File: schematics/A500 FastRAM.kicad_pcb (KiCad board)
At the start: 2 copper layers, 87.6 x 87.6 mm, 31 parts, among them J1 Microsemi_FlashPro-JTAG-10, U1 68000 Boardside, U10 TPS7333QP, U2 68000 Socket, U3 ATF1502ASV-15JU44, U4 74157, U5 74157, U6 IS41LV16100D, U7 IS41LV16100D, U8 IS41LV16100D, U9 IS41LV16100D

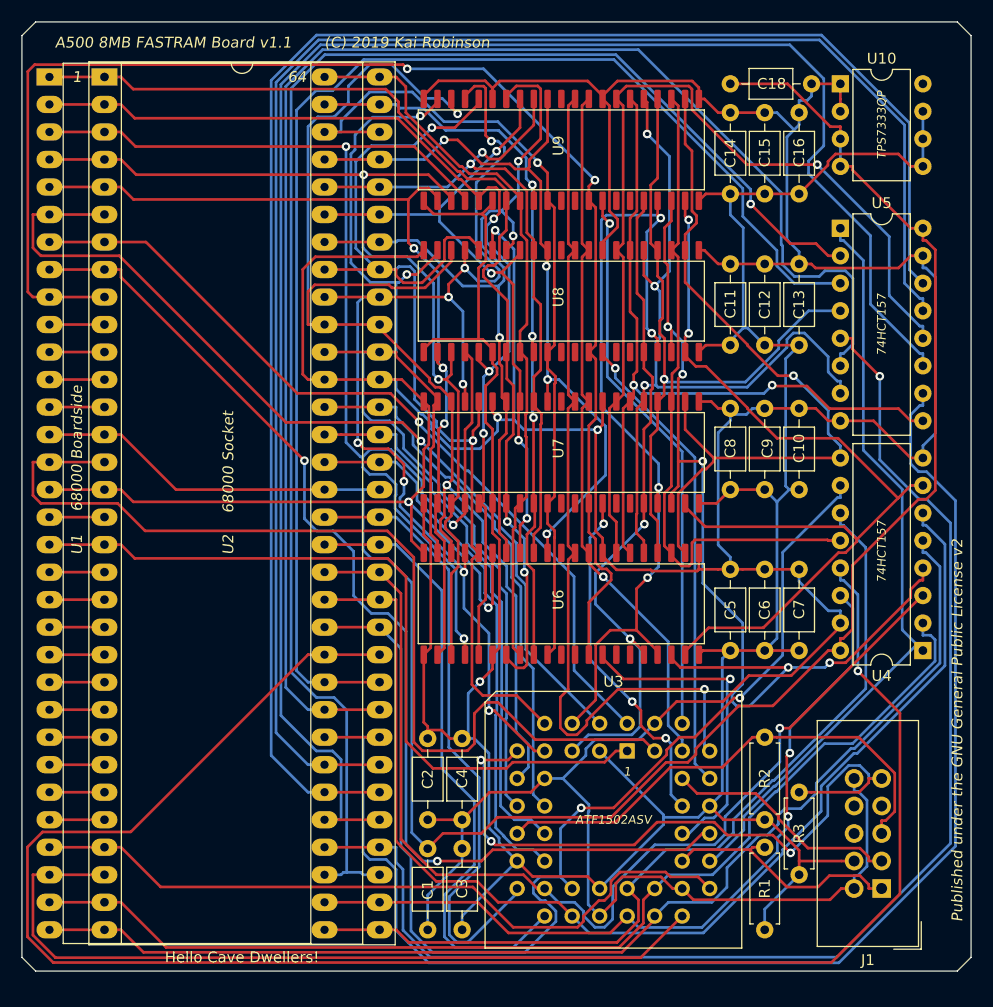
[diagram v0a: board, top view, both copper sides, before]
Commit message: Version 2
Swapped some components to SMD, reduced size of board - stepping stone to full blown accelerator integration!
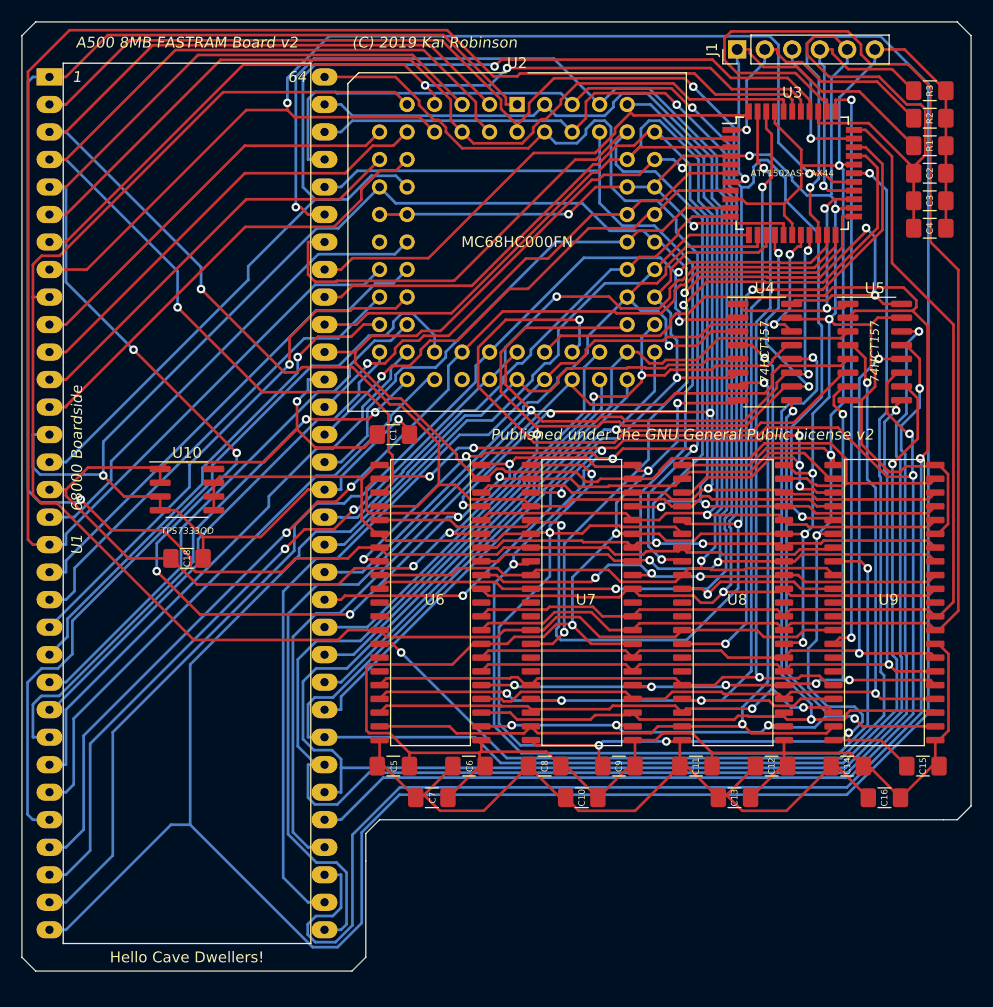
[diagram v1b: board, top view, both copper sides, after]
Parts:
- C1, C10, C11, C12, C13, C14, C15, C16, C18, C2, C3, C4, C5, C6, C7, C8, C9: footprint Capacitor_THT:C_Axial_L3.8mm_D2.6mm_P7.50mm_Horizontal -> Capacitor_SMD:C_1206_3216Metric_Pad1.42x1.75mm_HandSolder
- J1: value Microsemi_FlashPro-JTAG-10 -> Conn_01x06_Male; footprint Connector_IDC:IDC-Header_2x05_P2.54mm_Vertical -> Connector_PinHeader_2.54mm:PinHeader_1x06_P2.54mm_Vertical
- R1, R2, R3: footprint Resistor_THT:R_Axial_DIN0207_L6.3mm_D2.5mm_P7.62mm_Horizontal -> Resistor_SMD:R_1206_3216Metric_Pad1.42x1.75mm_HandSolder
- U10: value TPS7333QP -> TPS7333QD; footprint Package_DIP:DIP-8_W7.62mm -> Package_SO:SOIC-8_3.9x4.9mm_P1.27mm
- U2: value 68000 Socket -> MC68000FN; footprint Package_DIP:DIP-64_W25.4mm_Socket_LongPads -> Package_LCC:PLCC-68_THT-Socket
- U3: value ATF1502ASV-15JU44 -> ATF1502AS-7AX44; footprint Package_LCC:PLCC-44_THT-Socket -> Package_QFP:TQFP-44_10x10mm_P0.8mm
- U4, U5: footprint Package_DIP:DIP-16_W7.62mm -> Package_SO:SOIC-16_3.9x9.9mm_P1.27mm
- moved C3 80.0 mm to (201.9, 47.0), turned to 180 degrees
- moved J1 78.6 mm to (184.2, 33.0), turned to 90 degrees
- moved C2 75.6 mm to (201.9, 44.5), turned to 0 degrees
- moved R1 74.0 mm to (201.9, 41.9), turned to 180 degrees
- moved R3 73.4 mm to (201.9, 36.8), turned to 180 degrees
- moved U10 71.0 mm to (133.3, 73.7)
- moved C4 69.6 mm to (201.9, 49.5), turned to 0 degrees
- moved C18 66.6 mm to (133.3, 80.0), turned to 180 degrees
- moved R2 66.5 mm to (201.9, 39.4), turned to 180 degrees
- moved C16 56.3 mm to (197.7, 102.1), turned to 0 degrees
- moved U3 55.5 mm to (189.2, 44.5)
- moved C15 54.8 mm to (201.3, 99.2), turned to 0 degrees
- moved C14 53.9 mm to (194.3, 99.2), turned to 0 degrees
- moved U9 51.6 mm to (198.1, 82.5), turned to 0 degrees
- moved C13 42.2 mm to (183.9, 102.1), turned to 0 degrees
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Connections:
- J1 pad 1: /TCK -> /TMS
- J1 pad 2: GND -> /TDI
- J1 pad 4: /VCC33 -> /TCK
- J1 pad 5: /TMS -> GND
- J1 pad 6: Net-(J1-Pad6) -> /VCC33
- R1 pad 2: /TCK -> /TMS
- R2 pad 2: /TMS -> /TDI
- R3 pad 2: /TDI -> /TCK
- U2 pad 17: /CPU_HALT -> GND
- U2 pad 18: /CPU_RESET -> Net-(U2-Pad18)
- U2 pad 19: /CPU_VMA -> /CPU_HALT
- U2 pad 20: /CPU_E -> /CPU_RESET
- U2 pad 21: /CPU_VPA -> /CPU_VMA
- U2 pad 22: /CPU_BERR -> /CPU_E
- U2 pad 23: /CPU_IPL2 -> /CPU_VPA
- U2 pad 24: /CPU_IPL1 -> /CPU_BERR
- U2 pad 25: /CPU_IPL0 -> /CPU_IPL2
- U2 pad 26: /CPU_FC2 -> /CPU_IPL1
- U2 pad 27: /CPU_FC1 -> /CPU_IPL0
- U2 pad 28: /CPU_FC0 -> /CPU_FC2
- U2 pad 29: /CPU_A1 -> /CPU_FC1
- U2 pad 30: /CPU_A2 -> /CPU_FC0
- U2 pad 31: /CPU_A3 -> Net-(U2-Pad31)
- U2 pad 32: /CPU_A4 -> /CPU_A1
- U2 pad 33: /CPU_A5 -> /CPU_A2
- U2 pad 34: /CPU_A6 -> /CPU_A3
- U2 pad 35: /CPU_A7 -> /CPU_A4
- U2 pad 36: /CPU_A8 -> /CPU_A5
- U2 pad 37: /CPU_A9 -> /CPU_A6
- U2 pad 38: /CPU_A10 -> /CPU_A7
- U2 pad 39: /CPU_A11 -> /CPU_A8
- U2 pad 40: /CPU_A12 -> /CPU_A9
- U2 pad 41: /CPU_A13 -> /CPU_A10
- U2 pad 42: /CPU_A14 -> /CPU_A11
- U2 pad 43: /CPU_A15 -> /CPU_A12
- U2 pad 44: /CPU_A16 -> /CPU_A13
- U2 pad 45: /CPU_A17 -> /CPU_A14
- U2 pad 46: /CPU_A18 -> /CPU_A15
- U2 pad 47: /CPU_A19 -> /CPU_A16
- U2 pad 48: /CPU_A20 -> /CPU_A17
- U2 pad 49: VCC -> /CPU_A18
- U2 pad 50: /CPU_A21 -> /CPU_A19
- U2 pad 51: /CPU_A22 -> /CPU_A20
- U2 pad 52: /CPU_A23 -> VCC
- U2 pad 53: GND -> /CPU_A21
- U2 pad 54: /CPU_D15 -> /CPU_A22
- U2 pad 55: /CPU_D14 -> /CPU_A23
- U2 pad 56: /CPU_D13 -> GND
- U2 pad 57: /CPU_D12 -> GND
- U2 pad 58: /CPU_D11 -> /CPU_D15
- U2 pad 59: /CPU_D10 -> /CPU_D14
- U2 pad 60: /CPU_D9 -> /CPU_D13
- U2 pad 61: /CPU_D8 -> /CPU_D12
- U2 pad 62: /CPU_D7 -> /CPU_D11
- U2 pad 63: /CPU_D6 -> /CPU_D10
- U2 pad 64: /CPU_D5 -> /CPU_D9
- U3 pad 1: /CPU_RESET -> /TDI
- U3 pad 10: GND -> /CPU_A21
- U3 pad 11: /CPU_D15 -> /CPU_A20
- U3 pad 12: /CPU_A23 -> /CPU_A19
- U3 pad 13: /TMS -> /CPU_A18
- U3 pad 14: /CPU_A22 -> /CPU_A17
- U3 pad 15: /VCC33 -> /CPU_A16
- U3 pad 16: /CPU_A21 -> GND
- U3 pad 17: /CPU_A20 -> /VCC33
- U3 pad 18: /CPU_A19 -> /CPU_A6
- U3 pad 19: /CPU_A18 -> /CPU_A5
- U3 pad 2: /CPU_AS -> /CPU_D13
- U3 pad 20: /CPU_A17 -> /CPU_A4
- U3 pad 21: /CPU_A16 -> /CPU_A3
- U3 pad 22: GND -> /CPU_A2
- U3 pad 23: /VCC33 -> /CPU_A1
- U3 pad 24: /CPU_A6 -> GND
- U3 pad 25: /CPU_A5 -> /MUX_SWITCH
- U3 pad 26: /CPU_A4 -> /TCK
- U3 pad 27: /CPU_A3 -> /CPU_LDS
- U3 pad 28: /CPU_A2 -> /DRAM_RAS0
- U3 pad 29: /CPU_A1 -> /VCC33
- U3 pad 3: /VCC33 -> /CPU_D14
- U3 pad 30: GND -> /DRAM_RAS1
- U3 pad 31: /MUX_SWITCH -> /DRAM_RAS2
- U3 pad 32: /TCK -> /TDO
- U3 pad 33: /CPU_LDS -> /DRAM_LCAS
- U3 pad 34: /DRAM_RAS0 -> /DRAM_RAS3
- U3 pad 35: /VCC33 -> /DRAM_UCAS
- U3 pad 36: /DRAM_RAS1 -> GND
- U3 pad 37: /DRAM_RAS2 -> /CPU_CLK
- U3 pad 38: /TDO -> /CPU_UDS
- U3 pad 39: /DRAM_LCAS -> /CPU_RESET
- U3 pad 4: /DRAM_A1 -> GND
- U3 pad 40: /DRAM_RAS3 -> /CPU_AS
- U3 pad 41: /DRAM_UCAS -> /VCC33
- U3 pad 42: GND -> /DRAM_A1
- U3 pad 43: /CPU_CLK -> /DRAM_A0
- U3 pad 44: /CPU_UDS -> /CPU_D12
- U3 pad 5: /DRAM_A0 -> /CPU_D15
- U3 pad 6: /CPU_D12 -> /CPU_A23
- U3 pad 7: /TDI -> /TMS
- U3 pad 8: /CPU_D13 -> /CPU_A22
- U3 pad 9: /CPU_D14 -> /VCC33
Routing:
- net /CPU_A4: track 108.5 -> 272.6 mm, vias 0 -> 1
- net /CPU_D5: track 67.9 -> 204.5 mm, vias 0 -> 7
- net /CPU_D3: track 94.0 -> 213.2 mm, vias 3 -> 4
- net /CPU_A15: track 164.9 -> 61.5 mm, vias 1 -> 2
- net /CPU_D0: track 83.6 -> 176.2 mm, vias 3 -> 6
- net /CPU_RESET: track 71.5 -> 163.1 mm
- net /CPU_D10: track 62.7 -> 141.3 mm, vias 4 -> 3
- net /CPU_D1: track 93.1 -> 168.5 mm, vias 2 -> 8
- net /DRAM_RAS0: track 29.9 -> 105.2 mm, vias 1 -> 2
- net /CPU_D4: track 97.1 -> 168.4 mm, vias 2 -> 1
- net /CPU_A13: track 140.5 -> 70.8 mm, vias 0 -> 1
- net /DRAM_UCAS: track 65.4 -> 132.7 mm, vias 1 -> 0
- net /CPU_FC0: track 5.08 -> 71.5 mm
- net /CPU_D8: track 71.3 -> 135.8 mm, vias 4 -> 2
- net /CPU_A14: track 122.9 -> 65.0 mm
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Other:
- outline, holes or cut-outs redrawn
- board text added: "A500 8MB FASTRAM Board v2"
- board text added: "ATF1502AS-7AX44"
- board text added: "MC68HC000FN"
- board text added: "TPS7333QD"
- board text removed: "1"
- board text removed: "A500 8MB FASTRAM Board v1.1"
- board text removed: "ATF1502ASV"
- board text removed: "TPS7333QP"
